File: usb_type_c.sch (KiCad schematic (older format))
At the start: 3 parts, among them J1 TYPE_C_2

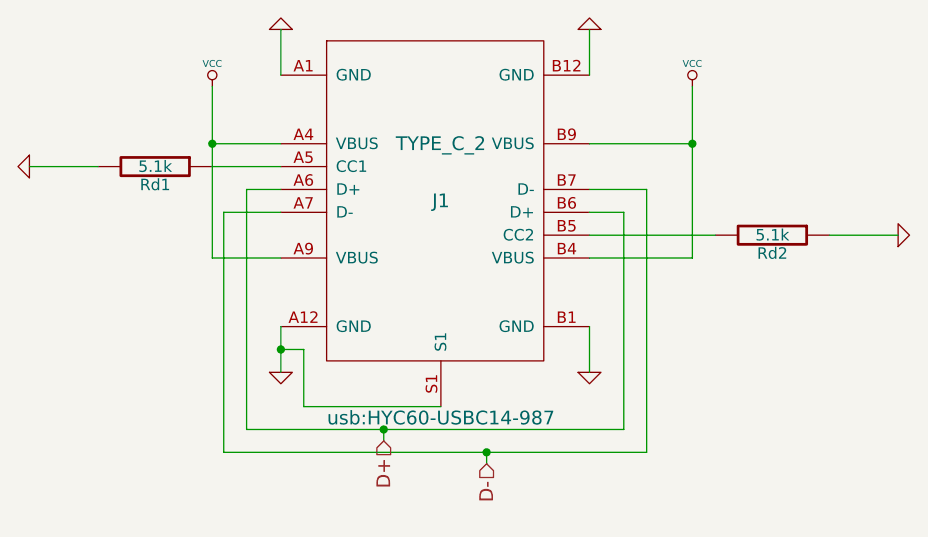
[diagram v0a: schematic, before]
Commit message: 增加一列F功能区 增加TrackPiont模块,同时增加ffc排线接口 右移右侧键布局
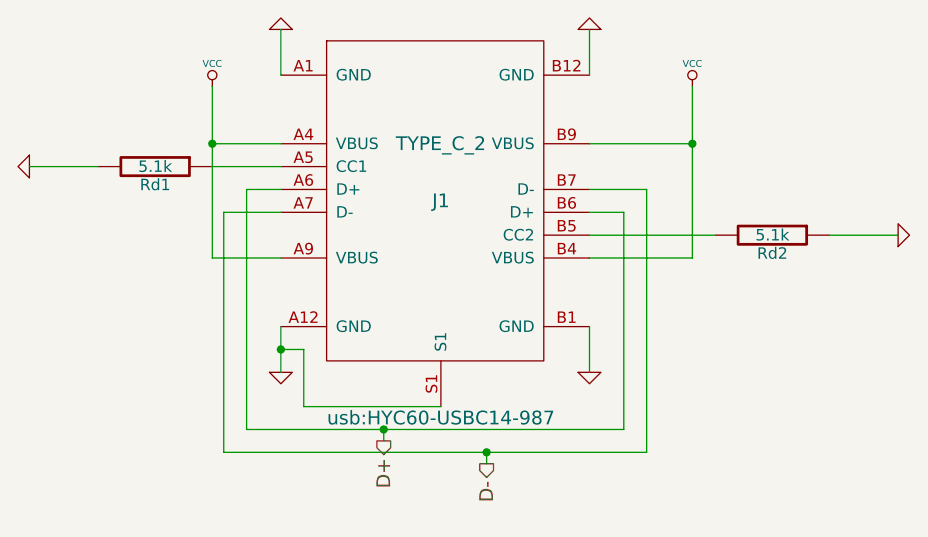
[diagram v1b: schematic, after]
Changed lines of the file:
@@
 Wire Wire Line
 	6300 4100 6050 4100
-Text HLabel 5150 5200 3    60   Input ~ 0
+Text HLabel 5150 5200 3    60   Output ~ 0
 D+
-Text HLabel 5600 5300 3    60   Input ~ 0
+Text HLabel 5600 5300 3    60   Output ~ 0
 D-
 Wire Wire Line
